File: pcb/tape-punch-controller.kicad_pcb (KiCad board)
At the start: 2 copper layers, 100 x 57 mm, 154 parts, among them J1 DB25_Male_MountingHoles, J2 Conn_01x03, J3 Conn_02x03_Odd_Even, J4 Conn_01x04, J5 USB_B, J6 Conn_01x16, J7 Conn_01x06, Q1 IRLZ44N, Q10 IRLML0060, Q2 IRLZ44N, Q3 IRLZ44N, Q4 IRLZ44N, Q5 IRLZ44N, Q6 IRLZ44N, Q7 IRLZ44N, Q8 IRLZ44N, Q9 IRLZ44N, SW1 SW_Push, U1 ATXMEGA192C3-AU, U2 LM321, U3 USBLC6-2SC6, U4 TSR_1-2433, U5 TSR_1-24150

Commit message: Version 2 PCB design (WIP)
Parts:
- removed MP1, MP2, MP3: Screw_Terminal_01x01, Mounting_Holes:MountingHole_4.3mm_M4_Pad
- removed TP63: TEST, Measurement_Points:Measurement_Point_Round-SMD-Pad_Small
- added J8: Conn_01x04, Pin_Headers:Pin_Header_Straight_1x04_Pitch2.54mm, B.Cu at (53.3, 113.7)
- added MH1: Screw_Terminal_01x01, Mounting_Holes:MountingHole_4.3mm_M4_Pad_Via, B.Cu at (94.0, 108.0)
- added MH2: Screw_Terminal_01x01, Mounting_Holes:MountingHole_4.3mm_M4_Pad_Via, B.Cu at (227.0, 111.0)
- added MH3: Screw_Terminal_01x01, Mounting_Holes:MountingHole_4.3mm_M4_Pad_Via, B.Cu at (95.0, 21.0)
- added MH4: Screw_Terminal_01x01, Mounting_Holes:MountingHole_4.3mm_M4_Pad_Via, B.Cu at (158.8, 63.5)
- C1, C14, C15, C2, C3, C4, C5, C6, C7, D1, D2, D3, Q10, R15, R16, R17, R18, R19, R21, R22, R23, R24, R34, R39, R4, R40, R42, R44, SW1, U1, U2, U3, U4, U5: moved to B.Cu
- C10: value 4.7n -> 10u; footprint Capacitors_SMD:C_0805_HandSoldering -> Capacitors_SMD:C_1206_HandSoldering; moved to B.Cu
- C11: footprint Capacitors_SMD:C_0805_HandSoldering -> Capacitors_SMD:C_1206_HandSoldering; moved to B.Cu
- C12, C13: value 10u -> 100n; moved to B.Cu
- C8: value 100n -> 4.7n; moved to B.Cu
- C9: value 100n -> 10u; footprint Capacitors_SMD:C_0805_HandSoldering -> Capacitors_SMD:C_1206_HandSoldering; moved to B.Cu
- J1: value DB25_Male_MountingHoles -> Conn_01x06; footprint local:NORCOMP_182-025-113R171 -> Local:Amphenol_T821106A1S100CEU; moved to B.Cu
- J2: value Conn_01x03 -> Conn_01x09; footprint local:Multicomp_MC000049 -> Local:Weidmuller_1234610000; moved to B.Cu
- J3: value Conn_02x03_Odd_Even -> USB_B; footprint Pin_Headers:Pin_Header_Straight_2x03_Pitch2.54mm -> Local:Multicomp_MC32597
- J4: value Conn_01x04 -> Conn_01x16; footprint Pin_Headers:Pin_Header_Straight_1x04_Pitch2.54mm -> Local:Amphenol_T821116A1S100CEU; moved to B.Cu
- J5: value USB_B -> Conn_01x06; footprint Connectors:USB_B -> Local:Amphenol_T821106A1S100CEU; moved to B.Cu
- J6: value Conn_01x16 -> Conn_01x02; footprint local:Amphenol_T821116A1S100CEU -> Local:Multicomp_MC000048; moved to B.Cu
- J7: value Conn_01x06 -> Conn_02x03_Odd_Even; footprint local:Amphenol_T821106A1S100CEU -> Pin_Headers:Pin_Header_Straight_2x03_Pitch2.54mm; moved to B.Cu
- Q1, Q2, Q3, Q4, Q5, Q6, Q7, Q8, Q9: value IRLZ44N -> IRLML0060; footprint TO_SOT_Packages_THT:TO-220-3_Vertical -> TO_SOT_Packages_SMD:SOT-23_Handsoldering; moved to B.Cu
- R1: value 68k -> 1M; moved to B.Cu
- R10: value 180 -> 10k; moved to B.Cu
- R11, R12, R13, R14, R20: value 180 -> 1M; moved to B.Cu
- R2: value 68k -> 1k; moved to B.Cu
- R25: value 120 -> 180; footprint Resistors_SMD:R_1210_HandSoldering -> Resistors_SMD:R_0805_HandSoldering; moved to B.Cu
- R26, R27: value 1k -> 180; moved to B.Cu
- R28: value 10k -> 180; moved to B.Cu
- R29: value 68k -> 180; moved to B.Cu
- R3: value 10k -> 1k; moved to B.Cu
- R30: value 18k -> 180; moved to B.Cu
- R31: value 1M -> 68k; moved to B.Cu
- R32: value 1k -> 18k; moved to B.Cu
- R33: value 1k -> 120; footprint Resistors_SMD:R_0805_HandSoldering -> Resistors_SMD:R_1210_HandSoldering; moved to B.Cu
- R35: value 1.8k -> 10k; footprint Resistors_SMD:R_1210_HandSoldering -> Resistors_SMD:R_0805_HandSoldering; moved to B.Cu
- R36: value 820 -> 68k; footprint Resistors_SMD:R_1206_HandSoldering -> Resistors_SMD:R_0805_HandSoldering; moved to B.Cu
- R37: value 82 -> 68k; moved to B.Cu
- R38: value 6.8k -> 68; moved to B.Cu
- R41: value 68 -> 10k; moved to B.Cu
- R43: value 10k -> 68k; moved to B.Cu
- R45: value 68k -> 6.8k; moved to B.Cu
- R5: value 1M -> 1.8k; footprint Resistors_SMD:R_0805_HandSoldering -> Resistors_SMD:R_1210_HandSoldering; moved to B.Cu
- R6: value 1M -> 820; footprint Resistors_SMD:R_0805_HandSoldering -> Resistors_SMD:R_1206_HandSoldering; moved to B.Cu
- R7: value 1M -> 82; moved to B.Cu
- R8, R9: value 1M -> 1k; moved to B.Cu
- RV1, RV2: footprint local:Citec_CB10LV103M -> Local:Citec_CB10LV103M; moved to B.Cu
- TP10, TP11, TP12, TP13, TP14, TP15, TP16, TP17, TP18, TP19, TP2, TP20, TP21, TP22, TP23, TP24, TP25, TP26, TP27, TP28, TP29, TP3, TP30, TP31, TP32, TP33, TP34, TP35, TP36, TP37, TP38, TP39, TP4, TP40, TP41, TP42, TP43, TP44, TP45, TP46, TP47, TP48, TP49, TP5, TP50, TP51, TP52, TP53, TP54, TP55, TP56, TP57, TP58, TP59, TP6, TP60, TP61, TP62, TP7, TP8, TP9: moved to F.Cu
- moved TP56 247.2 mm to (-50.8, 55.9)
- moved TP62 241.8 mm to (-36.8, 54.6)
- moved TP7 240.8 mm to (-42.5, 45.7)
- moved TP38 233.7 mm to (-40.6, 55.9)
- moved TP3 232.3 mm to (-73.0, 48.9)
- moved TP2 225.9 mm to (-59.1, 44.5)
- moved TP57 224.6 mm to (-31.1, 48.3)
- moved TP49 221.1 mm to (-34.3, 48.3)
- moved TP29 219.8 mm to (-43.2, 29.2)
- moved TP6 218.8 mm to (-55.9, 36.8)
- moved TP48 218.5 mm to (-41.9, 47.6)
- moved TP14 218.0 mm to (-66.7, 55.2)
- moved TP9 217.0 mm to (-48.9, 54.0)
- moved TP59 212.6 mm to (-26.0, 48.9)
- moved TP58 212.4 mm to (-24.1, 52.7)
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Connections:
- C1 pad 1: LOW_TAPE -> +3V3
- C10 pad 2: /Microcontroller/USB_SHIELD -> +3V3
- C11 pad 2: USB_SENSE -> +15V
- C12 pad 1: GND -> LOW_TAPE
- C12 pad 2: +15V -> GND
- C13 pad 1: GND -> NO_TAPE
- C13 pad 2: +3V3 -> GND
- C2 pad 1: NO_TAPE -> +3V3
- C7 pad 1: +3V3 -> +15V
- C8 pad 1: +3V3 -> GND
- C8 pad 2: GND -> /Microcontroller/USB_SHIELD
- C9 pad 1: +15V -> GND
- C9 pad 2: GND -> USB_SENSE
- J1 pad 1: CODE1_SOL -> GND
- J1 pad 2: CODE2_SOL -> ENABLE_RELAY
- J1 pad 3: CODE3_SOL -> SYNC_COIL+
- J1 pad 4: CODE4_SOL -> SYNC_COIL-
- J1 pad 5: CODE5_SOL -> /TapePunchConnector/LOW_TAPE_RAW
- J1 pad 6: CODE6_SOL -> /TapePunchConnector/NO_TAPE_RAW
- J2 pad 1: GND -> CODE1_SOL
- J2 pad 2: TP_EARTH -> CODE2_SOL
- J2 pad 3: +28V -> CODE3_SOL
- J3 pad 1: PDI_DATA -> /Microcontroller/USB_VBUS
- J3 pad 2: +3V3 -> /Microcontroller/USB_UNP_D-
- J3 pad 3: Net-(J3-Pad3) -> /Microcontroller/USB_UNP_D+
- J3 pad 4: Net-(J3-Pad4) -> GND
- J3 pad 5: RESET_n/PDI_CLK -> /Microcontroller/USB_SHIELD
- J4 pad 1: +3V3 -> GND
- J4 pad 2: UART_RX -> +3V3
- J4 pad 3: UART_TX -> /Controls/LCD_V0
- J4 pad 4: GND -> LCD_RS
- J5 pad 1: /Microcontroller/USB_VBUS -> GND
- J5 pad 2: /Microcontroller/USB_UNP_D- -> Net-(J5-Pad2)
- J5 pad 3: /Microcontroller/USB_UNP_D+ -> Net-(J5-Pad3)
- J5 pad 4: GND -> Net-(J5-Pad4)
- J5 pad 5: /Microcontroller/USB_SHIELD -> /Controls/CONFIRM_n_RAW
- J6 pad 2: +3V3 -> +28V
- J7 pad 1: GND -> PDI_DATA
- J7 pad 2: Net-(J7-Pad2) -> +3V3
- J7 pad 5: /Controls/CONFIRM_n_RAW -> RESET_n/PDI_CLK
- J7 pad 6: /Controls/CANCEL_n_RAW -> GND
- Q1 pad 1: /SolenoidDrivers/CODE0_GATE -> /SolenoidDrivers/CODE1_GATE
- Q1 pad 2: CODE0_SOL -> GND
- Q1 pad 3: GND -> CODE1_SOL
- Q2 pad 1: /SolenoidDrivers/CODE1_GATE -> /SolenoidDrivers/CODE2_GATE
- Q2 pad 2: CODE1_SOL -> GND
- Q2 pad 3: GND -> CODE2_SOL
- Q3 pad 1: /SolenoidDrivers/CODE2_GATE -> /SolenoidDrivers/CODE3_GATE
- Q3 pad 2: CODE2_SOL -> GND
- Q3 pad 3: GND -> CODE3_SOL
- Q4 pad 1: /SolenoidDrivers/CODE3_GATE -> /SolenoidDrivers/CODE4_GATE
- Q4 pad 2: CODE3_SOL -> GND
- Q4 pad 3: GND -> CODE4_SOL
- Q5 pad 1: /SolenoidDrivers/FEED_GATE -> /SolenoidDrivers/CODE5_GATE
- Q5 pad 2: FEED_SOL -> GND
- Q5 pad 3: GND -> CODE5_SOL
- Q6 pad 1: /SolenoidDrivers/CODE4_GATE -> /SolenoidDrivers/CODE6_GATE
- Q6 pad 2: CODE4_SOL -> GND
- Q6 pad 3: GND -> CODE6_SOL
- Q7 pad 1: /SolenoidDrivers/CODE5_GATE -> /SolenoidDrivers/CODE7_GATE
- Q7 pad 2: CODE5_SOL -> GND
- Q7 pad 3: GND -> CODE7_SOL
- Q8 pad 1: /SolenoidDrivers/CODE6_GATE -> /SolenoidDrivers/CODE0_GATE
- Q8 pad 2: CODE6_SOL -> GND
- Q8 pad 3: GND -> CODE0_SOL
- Q9 pad 1: /SolenoidDrivers/CODE7_GATE -> /SolenoidDrivers/FEED_GATE
- Q9 pad 2: CODE7_SOL -> GND
- Q9 pad 3: GND -> FEED_SOL
- R1 pad 1: /TapePunchConnector/LOW_TAPE_RAW -> /Microcontroller/USB_SHIELD
- R1 pad 2: LOW_TAPE -> GND
- R10 pad 1: /SolenoidDrivers/CODE0_GATE -> GND
- R10 pad 2: CODE0_SIG -> Net-(R10-Pad2)
- R11 pad 1: /SolenoidDrivers/CODE1_GATE -> CODE1_SIG
- R11 pad 2: CODE1_SIG -> GND
- R12 pad 1: /SolenoidDrivers/CODE2_GATE -> CODE2_SIG
- R12 pad 2: CODE2_SIG -> GND
- R13 pad 1: /SolenoidDrivers/CODE3_GATE -> CODE3_SIG
- R13 pad 2: CODE3_SIG -> GND
- R14 pad 1: /SolenoidDrivers/FEED_GATE -> CODE4_SIG
- R14 pad 2: FEED_SIG -> GND
- R15 pad 1: CODE4_SIG -> CODE5_SIG
- R16 pad 1: CODE5_SIG -> CODE6_SIG
- R17 pad 1: CODE6_SIG -> CODE7_SIG
- R18 pad 1: CODE7_SIG -> CODE0_SIG
- R19 pad 1: ENABLE_SIG -> FEED_SIG
- R2 pad 1: /TapePunchConnector/NO_TAPE_RAW -> /Microcontroller/USB_VBUS
- R2 pad 2: NO_TAPE -> USB_SENSE
- R20 pad 1: /SolenoidDrivers/CODE4_GATE -> ENABLE_SIG
- R20 pad 2: CODE4_SIG -> GND
- R21 pad 1: /SolenoidDrivers/CODE5_GATE -> /SolenoidDrivers/CODE1_GATE
- R21 pad 2: CODE5_SIG -> CODE1_SIG
- R22 pad 1: /SolenoidDrivers/CODE6_GATE -> /SolenoidDrivers/CODE2_GATE
- R22 pad 2: CODE6_SIG -> CODE2_SIG
- R23 pad 1: /SolenoidDrivers/CODE7_GATE -> /SolenoidDrivers/CODE3_GATE
- R23 pad 2: CODE7_SIG -> CODE3_SIG
- R24 pad 1: ENABLE_SIG -> /SolenoidDrivers/CODE4_GATE
- R24 pad 2: /SolenoidDrivers/ENABLE_GATE -> CODE4_SIG
- R25 pad 1: /SolenoidDrivers/ENABLE_DRAIN -> /SolenoidDrivers/CODE5_GATE
- R25 pad 2: ENABLE_RELAY -> CODE5_SIG
- R26 pad 1: SYNC_COIL- -> /SolenoidDrivers/CODE6_GATE
- R26 pad 2: +15V -> CODE6_SIG
- R27 pad 1: GND -> /SolenoidDrivers/CODE7_GATE
- R27 pad 2: SYNC_COIL- -> CODE7_SIG
- R28 pad 1: GND -> /SolenoidDrivers/CODE0_GATE
- R28 pad 2: Net-(R28-Pad2) -> CODE0_SIG
- R29 pad 1: SYNC -> /SolenoidDrivers/FEED_GATE
- R29 pad 2: /FeedbackSignalProcessing/SYNC_RAW -> FEED_SIG
- R3 pad 1: +3V3 -> GND
- R3 pad 2: /TapePunchConnector/LOW_TAPE_RAW -> USB_SENSE
- R30 pad 1: SYNC -> ENABLE_SIG
- R30 pad 2: GND -> /SolenoidDrivers/ENABLE_GATE
- R31 pad 1: /Microcontroller/USB_SHIELD -> SYNC
- R31 pad 2: GND -> /FeedbackSignalProcessing/SYNC_RAW
- R32 pad 1: /Microcontroller/USB_VBUS -> SYNC
- R32 pad 2: USB_SENSE -> GND
- R33 pad 1: GND -> /SolenoidDrivers/ENABLE_DRAIN
- R33 pad 2: USB_SENSE -> ENABLE_RELAY
- R34 pad 1: RESET_n/PDI_CLK -> +3V3
- R34 pad 2: +3V3 -> /TapePunchConnector/LOW_TAPE_RAW
- R35 pad 1: +28V -> +3V3
- R35 pad 2: Net-(D1-Pad2) -> /TapePunchConnector/NO_TAPE_RAW
- R36 pad 1: +15V -> LOW_TAPE
- R36 pad 2: Net-(D2-Pad2) -> /TapePunchConnector/LOW_TAPE_RAW
- R37 pad 1: +3V3 -> NO_TAPE
- R37 pad 2: Net-(D3-Pad2) -> /TapePunchConnector/NO_TAPE_RAW
- R38 pad 1: +28V -> Net-(J5-Pad2)
- R38 pad 2: /Controls/LCD_BLA -> +3V3
- R39 pad 1: STAT_RED -> STAT_GRN
- R39 pad 2: Net-(J7-Pad4) -> Net-(J5-Pad3)
- R4 pad 1: +3V3 -> RESET_n/PDI_CLK
- R4 pad 2: /TapePunchConnector/NO_TAPE_RAW -> +3V3
- R40 pad 1: STAT_GRN -> STAT_RED
- R40 pad 2: Net-(J7-Pad3) -> Net-(J5-Pad4)
- R41 pad 1: Net-(J7-Pad2) -> /Controls/CONFIRM_n_RAW
- R42 pad 1: /Controls/CONFIRM_n_RAW -> /Controls/CANCEL_n_RAW
- R43 pad 1: /Controls/CANCEL_n_RAW -> CONFIRM_n
- R43 pad 2: +3V3 -> /Controls/CONFIRM_n_RAW
- R44 pad 1: CONFIRM_n -> CANCEL_n
- R44 pad 2: /Controls/CONFIRM_n_RAW -> /Controls/CANCEL_n_RAW
- R45 pad 1: CANCEL_n -> +28V
- R45 pad 2: /Controls/CANCEL_n_RAW -> /Controls/LCD_BLA
- R5 pad 1: CODE0_SIG -> +28V
- R5 pad 2: GND -> Net-(D1-Pad2)
- R6 pad 1: CODE1_SIG -> +15V
- R6 pad 2: GND -> Net-(D2-Pad2)
- R7 pad 1: CODE2_SIG -> +3V3
- R7 pad 2: GND -> Net-(D3-Pad2)
- R8 pad 1: CODE3_SIG -> SYNC_COIL-
- R8 pad 2: GND -> +15V
- R9 pad 1: FEED_SIG -> GND
- R9 pad 2: GND -> SYNC_COIL-
- RV1 pad 3: Net-(R28-Pad2) -> Net-(R10-Pad2)
- TP1 pad 1: LOW_TAPE -> PDI_DATA
- TP10 pad 1: /SolenoidDrivers/CODE0_GATE -> SYNC_COIL+
- TP11 pad 1: /SolenoidDrivers/CODE1_GATE -> /FeedbackSignalProcessing/SYNC_THRESHOLD
- TP12 pad 1: /SolenoidDrivers/CODE2_GATE -> /FeedbackSignalProcessing/SYNC_RAW
- TP13 pad 1: /SolenoidDrivers/CODE3_GATE -> SYNC
- TP14 pad 1: /SolenoidDrivers/FEED_GATE -> CODE0_SIG
- TP15 pad 1: CODE0_SOL -> CODE1_SIG
- TP16 pad 1: CODE1_SOL -> CODE2_SIG
- TP17 pad 1: CODE2_SOL -> CODE3_SIG
- TP18 pad 1: CODE3_SOL -> FEED_SIG
- TP19 pad 1: FEED_SOL -> /SolenoidDrivers/CODE0_GATE
- TP2 pad 1: NO_TAPE -> RESET_n/PDI_CLK
- TP20 pad 1: CODE4_SIG -> /SolenoidDrivers/CODE1_GATE
- TP21 pad 1: CODE5_SIG -> /SolenoidDrivers/CODE2_GATE
- TP22 pad 1: CODE6_SIG -> /SolenoidDrivers/CODE3_GATE
- TP23 pad 1: CODE7_SIG -> /SolenoidDrivers/FEED_GATE
- TP24 pad 1: ENABLE_SIG -> CODE0_SOL
- TP25 pad 1: /SolenoidDrivers/CODE4_GATE -> CODE1_SOL
- TP26 pad 1: /SolenoidDrivers/CODE5_GATE -> CODE2_SOL
- TP27 pad 1: /SolenoidDrivers/CODE6_GATE -> CODE3_SOL
- TP28 pad 1: /SolenoidDrivers/CODE7_GATE -> FEED_SOL
- TP29 pad 1: /SolenoidDrivers/ENABLE_GATE -> CODE4_SIG
- TP3 pad 1: /TapePunchConnector/LOW_TAPE_RAW -> /Microcontroller/USB_VBUS
- TP30 pad 1: CODE4_SOL -> CODE5_SIG
- TP31 pad 1: CODE5_SOL -> CODE6_SIG
- TP32 pad 1: CODE6_SOL -> CODE7_SIG
- TP33 pad 1: CODE7_SOL -> ENABLE_SIG
- TP34 pad 1: ENABLE_RELAY -> /SolenoidDrivers/CODE4_GATE
- TP35 pad 1: /SolenoidDrivers/ENABLE_DRAIN -> /SolenoidDrivers/CODE5_GATE
- TP36 pad 1: PDI_DATA -> /SolenoidDrivers/CODE6_GATE
- TP37 pad 1: RESET_n/PDI_CLK -> /SolenoidDrivers/CODE7_GATE
- TP38 pad 1: /Microcontroller/USB_VBUS -> /SolenoidDrivers/ENABLE_GATE
- TP39 pad 1: USB_SENSE -> CODE4_SOL
- TP4 pad 1: /TapePunchConnector/NO_TAPE_RAW -> USB_SENSE
- TP40 pad 1: +28V -> CODE5_SOL
- TP41 pad 1: TP_EARTH -> CODE6_SOL
- TP42 pad 1: GND -> CODE7_SOL
- TP43 pad 1: +15V -> ENABLE_RELAY
- TP44 pad 1: +3V3 -> /SolenoidDrivers/ENABLE_DRAIN
- TP45 pad 1: SYNC_COIL- -> /TapePunchConnector/LOW_TAPE_RAW
- TP46 pad 1: SYNC_COIL+ -> /TapePunchConnector/NO_TAPE_RAW
- TP47 pad 1: /FeedbackSignalProcessing/SYNC_THRESHOLD -> LOW_TAPE
- TP48 pad 1: /FeedbackSignalProcessing/SYNC_RAW -> NO_TAPE
- TP49 pad 1: SYNC -> /Controls/CONFIRM_n_RAW
- TP5 pad 1: CODE0_SIG -> +28V
- TP50 pad 1: /Controls/CONFIRM_n_RAW -> /Controls/CANCEL_n_RAW
- TP51 pad 1: /Controls/CANCEL_n_RAW -> CONFIRM_n
- TP52 pad 1: CONFIRM_n -> CANCEL_n
- TP53 pad 1: CANCEL_n -> STAT_GRN
- TP54 pad 1: STAT_GRN -> STAT_RED
- TP55 pad 1: STAT_RED -> LCD_RS
- TP56 pad 1: LCD_RS -> LCD_E
- TP57 pad 1: LCD_E -> /Controls/LCD_V0
- TP58 pad 1: LCD_DB4 -> /Controls/LCD_BLA
- TP59 pad 1: LCD_DB5 -> LCD_DB4
- TP6 pad 1: CODE1_SIG -> GND
- TP60 pad 1: LCD_DB6 -> LCD_DB5
- TP61 pad 1: LCD_DB7 -> LCD_DB6
- TP62 pad 1: /Controls/LCD_V0 -> LCD_DB7
- TP7 pad 1: CODE2_SIG -> +3V3
- TP8 pad 1: CODE3_SIG -> +15V
- TP9 pad 1: FEED_SIG -> SYNC_COIL-
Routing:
- net +3V3: track 194.5 -> 16.8 mm, vias 7 -> 0
- net +15V: track 124.4 -> 11.6 mm, vias 4 -> 0
- net TP_EARTH: track 83.4 -> 0.00 mm
- net +28V: track 76.7 -> 0.00 mm
- net GND: track 69.1 -> 0.00 mm, vias 23 -> 0
- net CODE7_SIG: track 67.3 -> 2.54 mm, vias 2 -> 0
- net CODE5_SIG: track 61.0 -> 2.54 mm, vias 2 -> 0
- net /TapePunchConnector/NO_TAPE_RAW: track 55.4 -> 3.09 mm, vias 2 -> 0
- net CODE3_SIG: track 53.4 -> 2.54 mm, vias 2 -> 0
- net CODE0_SIG: track 51.5 -> 2.54 mm, vias 2 -> 0
- net /FeedbackSignalProcessing/SYNC_THRESHOLD: track 48.7 -> 0.00 mm, vias 1 -> 0
- net SYNC_COIL-: track 50.7 -> 3.65 mm
- net /Controls/LCD_V0: track 46.8 -> 0.00 mm
- net CODE6_SIG: track 48.9 -> 2.54 mm, vias 2 -> 0
- net CODE4_SIG: track 46.7 -> 2.54 mm, vias 2 -> 0
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- removed copper zone on B.Cu, net +28V
- removed copper zone on F.Cu, net +28V
- removed copper zone on F.Cu, net +3V3
- removed copper zone on F.Cu, net GND
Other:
- board outline removed
- net class 1A removed
- net class Mains earth removed
- net class Power added: clearance 0.2, trace_width 0.5, via_dia 1, via_drill 0.7
- net class Signal removed
- net class USB removed
- rule pad_to_mask_clearance: 0.2 -> 0
- board text removed: "0V,EARTH,28V"
- board text removed: "15V"
- board text removed: "28V"
- board text removed: "3V3"
- board text removed: "BUTTONS & LEDS"
- board text removed: "CONTRAST"
- board text removed: "Kier Davis me@kierdavis.com Dec 17"
- board text removed: "LCD"
- board text removed: "PDI"
- board text removed: "RESET"
- board text removed: "SERIAL"
- board text removed: "THRESHLD"

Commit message: Finish draft of second version of PCB
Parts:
- removed MH4: Screw_Terminal_01x01, Mounting_Holes:MountingHole_4.3mm_M4_Pad_Via
- MH1, MH2, MH3: footprint Mounting_Holes:MountingHole_4.3mm_M4_Pad_Via -> Mounting_Holes:MountingHole_4.3mm_M4_Pad
- TP1: moved to F.Cu
- moved TP3 211.0 mm to (134.0, 89.5)
- moved TP4 202.0 mm to (143.5, 100.3)
- moved TP56 200.6 mm to (147.3, 87.6)
- moved TP14 193.2 mm to (125.7, 73.0)
- moved TP18 192.6 mm to (130.2, 34.9)
- moved TP32 189.9 mm to (127.6, 64.8)
- moved TP57 189.7 mm to (154.9, 85.1)
- moved TP62 189.1 mm to (147.3, 97.8)
- moved TP2 187.5 mm to (127.6, 62.2)
- moved TP49 187.5 mm to (153.0, 40.6)
- moved TP59 186.8 mm to (154.9, 95.2)
- moved TP61 186.3 mm to (154.9, 97.8)
- moved TP50 185.8 mm to (150.5, 40.6)
- moved TP58 185.3 mm to (154.9, 100.3)
- moved TP31 183.5 mm to (128.9, 71.8)
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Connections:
- U1 pad 1: GND -> STAT_GRN
- U1 pad 12: GND -> LCD_RS
- U1 pad 13: GND -> LCD_E
- U1 pad 2: GND -> STAT_RED
- U1 pad 20: LCD_E -> USB_SENSE
- U1 pad 21: LCD_RS -> GND
- U1 pad 22: STAT_GRN -> GND
- U1 pad 23: STAT_RED -> GND
- U1 pad 36: CONFIRM_n -> GND
- U1 pad 37: CANCEL_n -> GND
- U1 pad 38: SYNC -> GND
- U1 pad 39: USB_SENSE -> SYNC
- U1 pad 40: LOW_TAPE -> NO_TAPE
- U1 pad 41: NO_TAPE -> LOW_TAPE
- U1 pad 43: FEED_SIG -> GND
- U1 pad 62: GND -> FEED_SIG
- U1 pad 63: GND -> CANCEL_n
- U1 pad 64: GND -> CONFIRM_n
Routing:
- net +3V3: track 16.8 -> 228.5 mm, vias 0 -> 5
- net +15V: track 11.6 -> 114.8 mm, vias 0 -> 1
- net FEED_SIG: track 2.54 -> 75.6 mm, vias 0 -> 2
- net /Controls/LCD_BLA: track 9.62 -> 82.2 mm
- net RESET_n/PDI_CLK: track 0.00 -> 57.0 mm, vias 0 -> 2
- net STAT_RED: track 0.00 -> 44.4 mm, vias 0 -> 2
- net +28V: track 0.00 -> 43.5 mm, vias 0 -> 1
- net STAT_GRN: track 0.00 -> 42.9 mm, vias 0 -> 2
- net CANCEL_n: track 0.00 -> 42.6 mm, vias 0 -> 2
- net CODE7_SIG: track 2.54 -> 43.5 mm, vias 0 -> 2
- net CODE0_SIG: track 2.54 -> 43.0 mm, vias 0 -> 2
- net UART_RX: track 0.00 -> 37.9 mm, vias 0 -> 1
- net CONFIRM_n: track 0.00 -> 37.6 mm, vias 0 -> 2
- net UART_TX: track 0.00 -> 36.7 mm, vias 0 -> 1
- net ENABLE_SIG: track 2.54 -> 36.6 mm, vias 0 -> 2
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- added copper zone on F.Cu, net GND
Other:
- board outline added: 70 x 88 mm
- board text added: "+"
- board text added: "-"
- board text added: "15V"
- board text added: "28V"
- board text added: "28V in"
- board text added: "3.3V"
- board text added: "C0"
- board text added: "C1"
- board text added: "C2"
- board text added: "C3"
- board text added: "C4"
- board text added: "C5"
- board text added: "C6"
- board text added: "C7"
- board text added: "CLK"
- board text added: "CONTRAST"
- board text added: "DAT"
- board text added: "F"
- board text added: "GND"
- board text added: "Kier Davis 2018/01 me@kierdavis.com"
- board text added: "LCD"
- board text added: "LEDS/BTNS"
- board text added: "NC"
- board text added: "PDI"
- board text added: "RESET"
- board text added: "RX"
- board text added: "TAPE PNCH"
- board text added: "THRESHOLD"
- board text added: "TX"
- board text added: "UART"

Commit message: Work on PCB design
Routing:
- net GND: track 30.1 -> 28.4 mm
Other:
- outline, holes or cut-outs redrawn
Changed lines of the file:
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@@
     (links 287)
     (no_connects 0)
-    (area 91.949999 19.949999 162.050001 108.050001)
+    (area 89.371428 18 164.628573 110.000001)
     (thickness 1.6)
-    (drawings 60)
-    (tracks 722)
+    (drawings 68)
+    (tracks 721)
     (zones 0)
     (modules 154)
@@
   (page A4)
   (layers
-    (0 F.Cu signal)
+    (0 F.Cu signal hide)
     (31 B.Cu signal)
     (32 B.Adhes user)
@@
     (user_trace_width 4)
     (trace_clearance 0.2)
-    (zone_clearance 0.3)
+    (zone_clearance 0.25)
     (zone_45_only yes)
     (trace_min 0.125)
@@
       (net 4 /Microcontroller/USB_SHIELD))
   )
+  (gr_arc (start 156 26) (end 156 20) (angle 90) (layer Edge.Cuts) (width 0.1))
+  (gr_arc (start 98 26) (end 92 26) (angle 90) (layer Edge.Cuts) (width 0.1))
+  (gr_arc (start 98 102) (end 98 108) (angle 90) (layer Edge.Cuts) (width 0.1))
+  (gr_arc (start 156 102) (end 162 102) (angle 90) (layer Edge.Cuts) (width 0.1))
+  (gr_arc (start 98 26) (end 93 26) (angle 90) (layer Margin) (width 0.2))
+  (gr_arc (start 156 26) (end 156 21) (angle 90) (layer Margin) (width 0.2))
+  (gr_arc (start 156 102) (end 161 102) (angle 90) (layer Margin) (width 0.2))
+  (gr_arc (start 98 102) (end 98 107) (angle 90) (layer Margin) (width 0.2))
   (gr_line (start 127.635 102.235) (end 127.635 103.505) (angle 90) (layer B.SilkS) (width 0.2))
   (gr_line (start 125.095 102.235) (end 127.635 102.235) (angle 90) (layer B.SilkS) (width 0.2))
@@
     (effects (font (size 2 2) (thickness 0.3)) (justify left mirror))
   )
-  (gr_line (start 92 20) (end 162 20) (angle 90) (layer Edge.Cuts) (width 0.1))
-  (gr_line (start 92 108) (end 92 20) (angle 90) (layer Edge.Cuts) (width 0.1))
-  (gr_line (start 162 108) (end 92 108) (angle 90) (layer Edge.Cuts) (width 0.1))
-  (gr_line (start 162 20) (end 162 108) (angle 90) (layer Edge.Cuts) (width 0.1))
+  (gr_line (start 98 20) (end 156 20) (angle 90) (layer Edge.Cuts) (width 0.1))
+  (gr_line (start 92 26) (end 92 102) (angle 90) (layer Edge.Cuts) (width 0.1))
+  (gr_line (start 98 108) (end 156 108) (angle 90) (layer Edge.Cuts) (width 0.1))
+  (gr_line (start 162 26) (end 162 102) (angle 90) (layer Edge.Cuts) (width 0.1))
   (gr_text RESET (at 158.75 49.53 90) (layer B.SilkS)
     (effects (font (size 2 2) (thickness 0.4)) (justify mirror))
@@
     (effects (font (size 2 2) (thickness 0.4)) (justify mirror))
   )
-  (gr_line (start 93 107) (end 161 107) (angle 90) (layer Margin) (width 0.2))
-  (gr_line (start 161 21) (end 161 107) (angle 90) (layer Margin) (width 0.2))
-  (gr_line (start 93 21) (end 161 21) (angle 90) (layer Margin) (width 0.2))
-  (gr_line (start 93 21) (end 93 107) (angle 90) (layer Margin) (width 0.2))
+  (gr_line (start 98 107) (end 156 107) (angle 90) (layer Margin) (width 0.2))
+  (gr_line (start 161 26) (end 161 102) (angle 90) (layer Margin) (width 0.2))
+  (gr_line (start 98 21) (end 156 21) (angle 90) (layer Margin) (width 0.2))
+  (gr_line (start 93 26) (end 93 102) (angle 90) (layer Margin) (width 0.2))
+  (segment (start 149.86 82.55) (end 151.13 81.28) (width 0.5) (layer B.Cu) (net 1) (status 400000))
+  (segment (start 151.13 81.28) (end 151.13 73.025) (width 0.5) (layer B.Cu) (net 1))
   (segment (start 139.389141 68.889724) (end 139.374724 68.889724) (width 0.5) (layer B.Cu) (net 1))
   (segment (start 139.374724 68.889724) (end 135.255 64.77) (width 0.5) (layer B.Cu) (net 1))
@@
   (segment (start 153.63 74.85) (end 152.955 74.85) (width 0.5) (layer B.Cu) (net 1))
   (segment (start 152.955 74.85) (end 151.765 73.66) (width 0.5) (layer B.Cu) (net 1))
+  (segment (start 151.13 73.025) (end 151.765 73.66) (width 0.5) (layer B.Cu) (net 1))
   (segment (start 139.389141 68.889724) (end 146.994724 68.889724) (width 0.5) (layer B.Cu) (net 1))
-  (segment (start 146.994724 68.889724) (end 151.765 73.66) (width 0.5) (layer B.Cu) (net 1))
-  (segment (start 151.765 80.645) (end 149.86 82.55) (width 0.5) (layer B.Cu) (net 1))
-  (segment (start 151.765 73.66) (end 151.765 80.645) (width 0.5) (layer B.Cu) (net 1))
+  (segment (start 146.994724 68.889724) (end 151.13 73.025) (width 0.5) (layer B.Cu) (net 1))
   (segment (start 123.19 78.105) (end 123.825 77.47) (width 0.5) (layer F.Cu) (net 1))
   (segment (start 123.825 77.47) (end 124.46 78.105) (width 0.5) (layer F.Cu) (net 1))
@@
   (segment (start 146.05 86.36) (end 146.05 89.555) (width 0.5) (layer B.Cu) (net 1))
   (segment (start 145.535 85.845) (end 146.05 86.36) (width 0.5) (layer B.Cu) (net 1))
+  (segment (start 114.935 33.655) (end 119.38 38.1) (width 0.25) (layer B.Cu) (net 2) (status 400000))
+  (via (at 121.92 38.1) (size 0.6) (drill 0.4) (layers F.Cu B.Cu) (net 2))
+  (segment (start 120.015 38.1) (end 121.92 38.1) (width 0.25) (layer F.Cu) (net 2))
+  (via (at 120.015 38.1) (size 0.6) (drill 0.4) (layers F.Cu B.Cu) (net 2))
+  (segment (start 119.38 38.1) (end 120.015 38.1) (width 0.25) (layer B.Cu) (net 2))
   (segment (start 133.75 99.6) (end 137.16 96.19) (width 0.25) (layer F.Cu) (net 2))
   (via (at 137.16 93.98) (size 0.6) (drill 0.4) (layers F.Cu B.Cu) (net 2))
   (segment (start 137.16 96.19) (end 137.16 93.98) (width 0.25) (layer F.Cu) (net 2))
-  (segment (start 114.935 33.655) (end 115.57 33.655) (width 0.25) (layer B.Cu) (net 2))
-  (segment (start 115.57 33.655) (end 120.015 38.1) (width 0.25) (layer B.Cu) (net 2))
-  (via (at 120.015 38.1) (size 0.6) (drill 0.4) (layers F.Cu B.Cu) (net 2))
-  (segment (start 120.015 38.1) (end 121.92 38.1) (width 0.25) (layer F.Cu) (net 2))
-  (via (at 121.92 38.1) (size 0.6) (drill 0.4) (layers F.Cu B.Cu) (net 2))
   (segment (start 153.035 33.02) (end 154.94 33.02) (width 0.25) (layer B.Cu) (net 2))
   (segment (start 149.86 36.83) (end 148.59 38.1) (width 0.25) (layer B.Cu) (net 2))
   (segment (start 154.94 36.83) (end 149.86 36.83) (width 0.25) (layer B.Cu) (net 2))
   (segment (start 154.94 33.02) (end 154.94 36.83) (width 0.25) (layer B.Cu) (net 2))
-  (segment (start 128.27 94.06) (end 128.27 93.345) (width 0.25) (layer B.Cu) (net 2))
-  (segment (start 128.27 93.345) (end 127.635 92.71) (width 0.25) (layer B.Cu) (net 2))
   (segment (start 132.715 39.37) (end 132.715 41.91) (width 0.5) (layer F.Cu) (net 3))
   (segment (start 132.715 38.735) (end 130.81 36.83) (width 0.5) (layer F.Cu) (net 3))
@@
   (segment (start 139.7 46.99) (end 144.145 46.99) (width 0.25) (layer B.Cu) (net 8))
   (segment (start 144.78 46.355) (end 144.78 45.7) (width 0.25) (layer B.Cu) (net 8))
+  (segment (start 137.16 45.8) (end 138.51 44.45) (width 0.25) (layer B.Cu) (net 9) (status 400000))
+  (segment (start 140.99 44.45) (end 142.24 45.7) (width 0.25) (layer B.Cu) (net 9) (status 800000))
+  (segment (start 138.51 44.45) (end 140.99 44.45) (width 0.25) (layer B.Cu) (net 9))
   (segment (start 137.16 43.815) (end 136.525 44.45) (width 0.25) (layer F.Cu) (net 9))
   (segment (start 136.525 44.45) (end 136.525 46.355) (width 0.25) (layer F.Cu) (net 9))
@@
   (segment (start 137.795 46.435) (end 137.16 45.8) (width 0.25) (layer B.Cu) (net 9))
   (segment (start 137.24 45.8) (end 137.16 45.8) (width 0.25) (layer B.Cu) (net 9))
-  (segment (start 137.16 45.8) (end 138.51 44.45) (width 0.25) (layer B.Cu) (net 9))
-  (segment (start 140.99 44.45) (end 142.24 45.7) (width 0.25) (layer B.Cu) (net 9))
-  (segment (start 138.51 44.45) (end 140.99 44.45) (width 0.25) (layer B.Cu) (net 9))
   (segment (start 129.635 31.75) (end 128.985 31.1) (width 0.25) (layer B.Cu) (net 10))
   (segment (start 128.985 31.1) (end 128.985 28.575) (width 0.25) (layer B.Cu) (net 10))
@@
   )
   (zone (net 2) (net_name GND) (layer B.Cu) (hatch edge 0.508)
-    (connect_pads (clearance 0.3))
-    (min_thickness 0.3)
-    (fill yes (arc_segments 16) (thermal_gap 0.3) (thermal_bridge_width 0.5) (smoothing fillet) (radius 1))
+    (connect_pads (clearance 0.25))
+    (min_thickness 0.25)
+    (fill yes (arc_segments 16) (thermal_gap 0.25) (thermal_bridge_width 0.5) (smoothing fillet) (radius 1))
     (polygon
       (pts
@@
   )
   (zone (net 2) (net_name GND) (layer F.Cu) (hatch edge 0.508)
-    (connect_pads (clearance 0.3))
-    (min_thickness 0.3)
-    (fill yes (arc_segments 16) (thermal_gap 0.3) (thermal_bridge_width 0.5) (smoothing fillet) (radius 1))
+    (connect_pads (clearance 0.25))
+    (min_thickness 0.25)
+    (fill yes (arc_segments 16) (thermal_gap 0.25) (thermal_bridge_width 0.5) (smoothing fillet) (radius 1))
     (polygon
       (pts

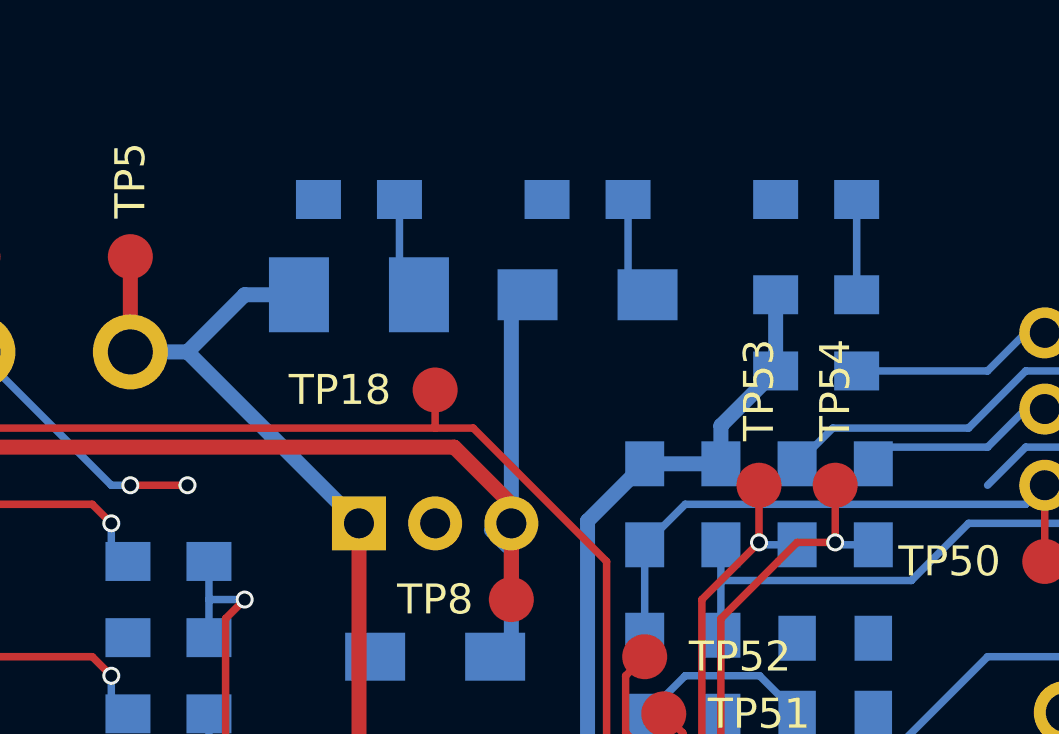
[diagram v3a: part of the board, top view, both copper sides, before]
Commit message: pcb: remove power LEDs
We have test points and an external power LED, so they're pretty
redundant. They're also quite power hungry (the resistor for the
28V LED would dissipate about 300mW constantly), and removing them
reduces the number of different types of component used on the
board considerably.
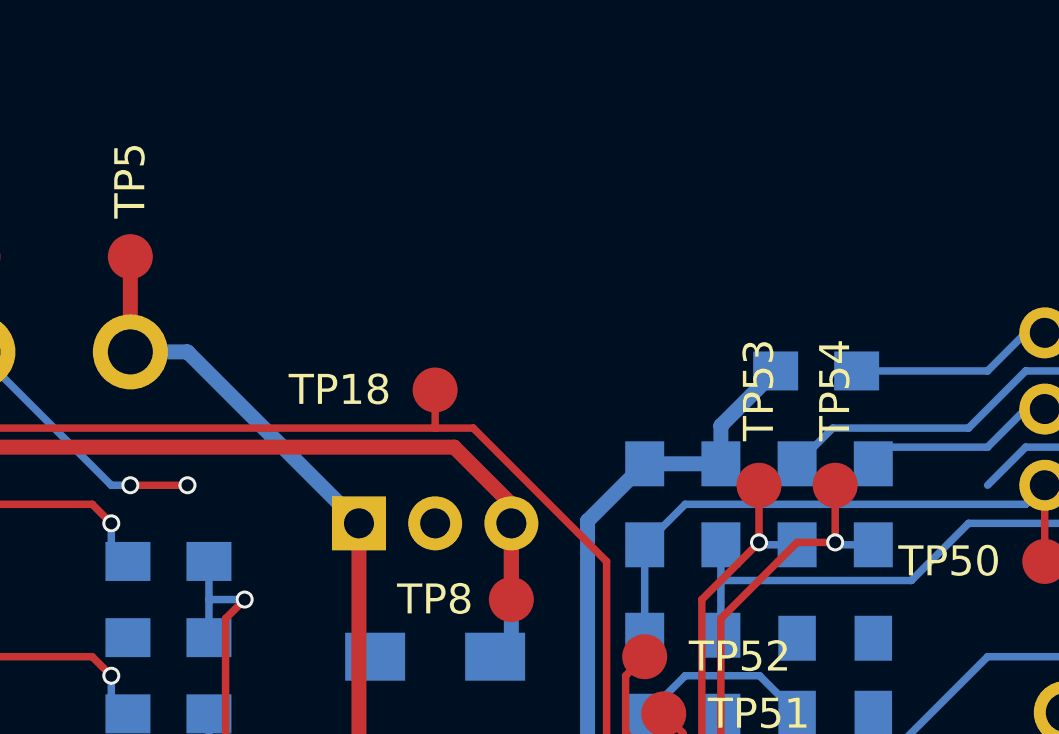
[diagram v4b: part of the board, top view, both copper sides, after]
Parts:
- removed D1, D2, D3: green, LEDs:LED_0805_HandSoldering
- removed R5: 1.8k, Resistors_SMD:R_1210_HandSoldering
- removed R6: 820, Resistors_SMD:R_1206_HandSoldering
- removed R7: 82, Resistors_SMD:R_0805_HandSoldering
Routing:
- net +15V: track 114.8 -> 105.4 mm
- net +28V: track 43.5 -> 39.0 mm
- net Net-(D2-Pad2): track 3.44 -> 0.00 mm
- net Net-(D1-Pad2): track 3.44 -> 0.00 mm
- net Net-(D3-Pad2): track 3.18 -> 0.00 mm
- net +3V3: track 228.9 -> 226.3 mm
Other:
- board text removed: "28V"
